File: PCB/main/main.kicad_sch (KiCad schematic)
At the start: 4 parts, among them J1 Conn_01x33_Female, J2 Conn_01x33_Female, J3 Conn_01x33_Female, J4 Conn_01x33_Female

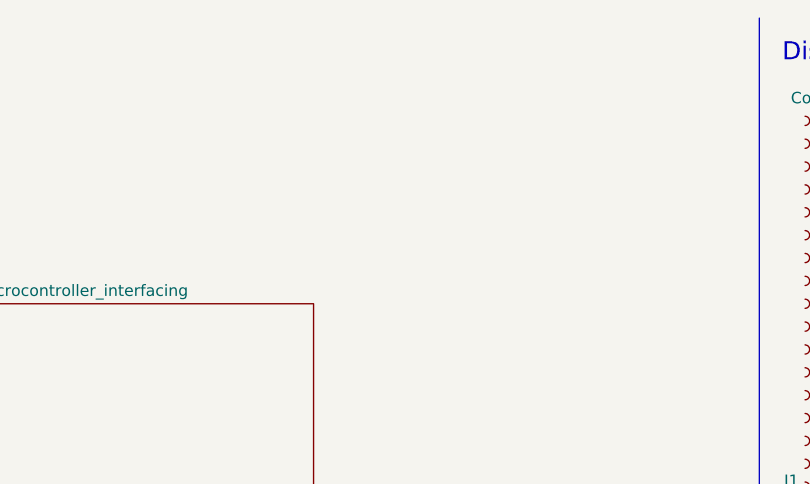
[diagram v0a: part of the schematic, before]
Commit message: Updated interfacing schem
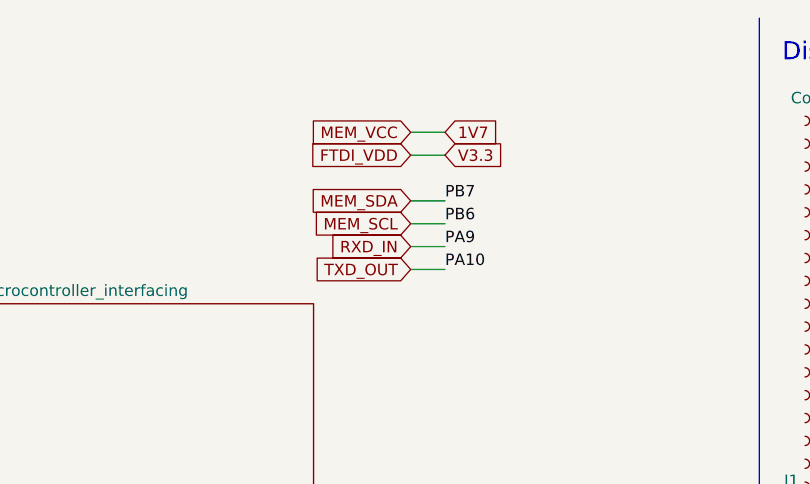
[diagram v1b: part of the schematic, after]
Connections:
- net PA10 renamed TXD_OUT
- net PA9 renamed RXD_IN
- net PB6 renamed MEM_SCL
- net PB7 renamed MEM_SDA
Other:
- title: EEE3088F Template -> EEE3088F Group 9
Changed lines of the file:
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@@
   (paper "A4")
   (title_block
-    (title "EEE3088F Template")
-    (date "2022-02-21")
-    (rev "V0.0")
+    (title "EEE3088F Group 9")
+    (date "2022-03-11")
+    (rev "V0.2")
     (company "University of Cape Town")
     (comment 3 "@Checked By: ")
-    (comment 4 "@Authors: Justin Pead")
+    (comment 4 "@Authors: David Young, Cameron Wilson, Caide Spriestersbach")
+  )
+  (wire (pts (xy 162.56 40.64) (xy 166.37 40.64))
+    (stroke (width 0) (type default) (color 0 0 0 0))
   )
   (wire (pts (xy 211.455 44.45) (xy 215.265 44.45))
     (stroke (width 0) (type default) (color 0 0 0 0))
   )
+  (wire (pts (xy 162.56 35.56) (xy 166.37 35.56))
+    (stroke (width 0) (type default) (color 0 0 0 0))
+  )
   (polyline (pts (xy 201.295 12.7) (xy 201.295 109.855))
     (stroke (width 0) (type default) (color 0 0 0 0))
@@
     (stroke (width 0) (type default) (color 0 0 0 0))
   )
+  (wire (pts (xy 162.56 38.1) (xy 166.37 38.1))
+    (stroke (width 0) (type default) (color 0 0 0 0))
+  )
   (wire (pts (xy 229.235 24.13) (xy 231.775 24.13))
     (stroke (width 0) (type default) (color 0 0 0 0))
@@
     (stroke (width 0) (type default) (color 0 0 0 0))
   )
+  (wire (pts (xy 162.56 27.94) (xy 166.37 27.94))
+    (stroke (width 0) (type default) (color 0 0 0 0))
+  )
+  (wire (pts (xy 162.56 33.02) (xy 166.37 33.02))
+    (stroke (width 0) (type default) (color 0 0 0 0))
+  )
   (wire (pts (xy 248.285 34.29) (xy 253.365 34.29))
+    (stroke (width 0) (type default) (color 0 0 0 0))
+  )
+  (wire (pts (xy 162.56 25.4) (xy 166.37 25.4))
     (stroke (width 0) (type default) (color 0 0 0 0))
   )
@@
     (effects (font (size 1.27 1.27)) (justify left bottom))
   )
+  (label "PA10" (at 166.37 40.64 0)
+    (effects (font (size 1.27 1.27)) (justify left bottom))
+  )
   (label "PC15" (at 211.455 36.83 0)
     (effects (font (size 1.27 1.27)) (justify left bottom))
@@
     (effects (font (size 1.27 1.27)) (justify left bottom))
   )
+  (label "PB6" (at 166.37 35.56 0)
+    (effects (font (size 1.27 1.27)) (justify left bottom))
+  )
   (label "PC0" (at 211.455 49.53 0)
     (effects (font (size 1.27 1.27)) (justify left bottom))
@@
     (effects (font (size 1.27 1.27)) (justify left bottom))
   )
+  (label "PB7" (at 166.37 33.02 0)
+    (effects (font (size 1.27 1.27)) (justify left bottom))
+  )
   (label "PA0" (at 229.235 59.69 0)
     (effects (font (size 1.27 1.27)) (justify left bottom))
@@
     (effects (font (size 1.27 1.27)) (justify left bottom))
   )
+  (label "PA9" (at 166.37 38.1 0)
+    (effects (font (size 1.27 1.27)) (justify left bottom))
+  )
   (label "PC9" (at 267.335 87.63 0)
     (effects (font (size 1.27 1.27)) (justify left bottom))
+  )
+  (global_label "FTDI_VDD" (shape input) (at 162.56 27.94 180) (fields_autoplaced)
+    (effects (font (size 1.27 1.27)) (justify right))
+    (property "Intersheet References" "${INTERSHEET_REFS}" (id 0) (at 151.6198 28.0194 0)
+      (effects (font (size 1.27 1.27)) (justify right) hide)
+    )
+  )
+  (global_label "1V7" (shape input) (at 166.37 25.4 0) (fields_autoplaced)
+    (effects (font (size 1.27 1.27)) (justify left))
+    (property "Intersheet References" "${INTERSHEET_REFS}" (id 0) (at 172.2907 25.3206 0)
+      (effects (font (size 1.27 1.27)) (justify left) hide)
+    )
+  )
+  (global_label "V3.3" (shape input) (at 166.37 27.94 0) (fields_autoplaced)
+    (effects (font (size 1.27 1.27)) (justify left))
+    (property "Intersheet References" "${INTERSHEET_REFS}" (id 0) (at 172.8955 27.8606 0)
+      (effects (font (size 1.27 1.27)) (justify left) hide)
+    )
+  )
+  (global_label "TXD_OUT" (shape input) (at 162.56 40.64 180) (fields_autoplaced)
+    (effects (font (size 1.27 1.27)) (justify right))
+    (property "Intersheet References" "${INTERSHEET_REFS}" (id 0) (at 152.1036 40.7194 0)
+      (effects (font (size 1.27 1.27)) (justify right) hide)
+    )
+  )
+  (global_label "RXD_IN" (shape input) (at 162.56 38.1 180) (fields_autoplaced)
+    (effects (font (size 1.27 1.27)) (justify right))
+    (property "Intersheet References" "${INTERSHEET_REFS}" (id 0) (at 153.4945 38.1794 0)
+      (effects (font (size 1.27 1.27)) (justify right) hide)
+    )
+  )
+  (global_label "MEM_VCC" (shape input) (at 162.56 25.4 180) (fields_autoplaced)
+    (effects (font (size 1.27 1.27)) (justify right))
+    (property "Intersheet References" "${INTERSHEET_REFS}" (id 0) (at 151.4988 25.3206 0)
+      (effects (font (size 1.27 1.27)) (justify right) hide)
+    )
+  )
+  (global_label "MEM_SCL" (shape input) (at 162.56 35.56 180) (fields_autoplaced)
+    (effects (font (size 1.27 1.27)) (justify right))
+    (property "Intersheet References" "${INTERSHEET_REFS}" (id 0) (at 151.6198 35.4806 0)
+      (effects (font (size 1.27 1.27)) (justify right) hide)
+    )
+  )
+  (global_label "MEM_SDA" (shape input) (at 162.56 33.02 180) (fields_autoplaced)
+    (effects (font (size 1.27 1.27)) (justify right))
+    (property "Intersheet References" "${INTERSHEET_REFS}" (id 0) (at 151.5593 32.9406 0)
+      (effects (font (size 1.27 1.27)) (justify right) hide)
+    )
   )
   (symbol (lib_id "power:GND") (at 233.045 105.41 90) (unit 1)
@@
       (reference "#PWR018") (unit 1) (value "GND") (footprint "")
     )
-    (path "/59b42903-2dc7-4011-ab5b-d7b81bd233c3/accade58-c1d2-4f6f-9fed-63e39d1d9928"
-      (reference "#PWR019") (unit 1) (value "GND") (footprint "")
-    )
     (path "/d15c8919-7ccc-44b2-8fc4-b04c1b47b6fa/dd448a84-e210-4674-86a8-ae65df0106f1"
       (reference "#PWR020") (unit 1) (value "GND") (footprint "")
@@
       (reference "R13") (unit 1) (value "4.7k") (footprint "")
     )
-    (path "/59b42903-2dc7-4011-ab5b-d7b81bd233c3/97b86286-2603-4849-bdd6-1cfc0a30163c"
-      (reference "R14") (unit 1) (value "10k") (footprint "")
-    )
     (path "/d15c8919-7ccc-44b2-8fc4-b04c1b47b6fa/0e943f16-1e71-4694-b072-e169f2da7d03"

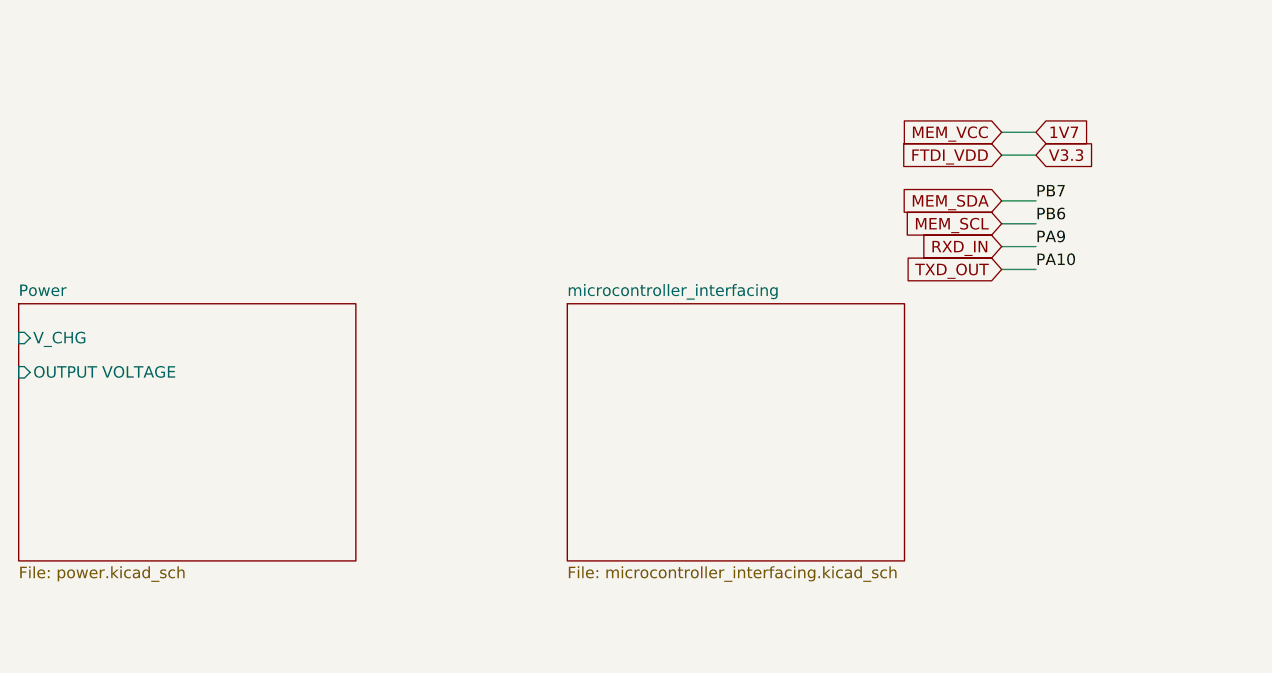
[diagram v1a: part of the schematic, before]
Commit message: Finished initial interfacing schem
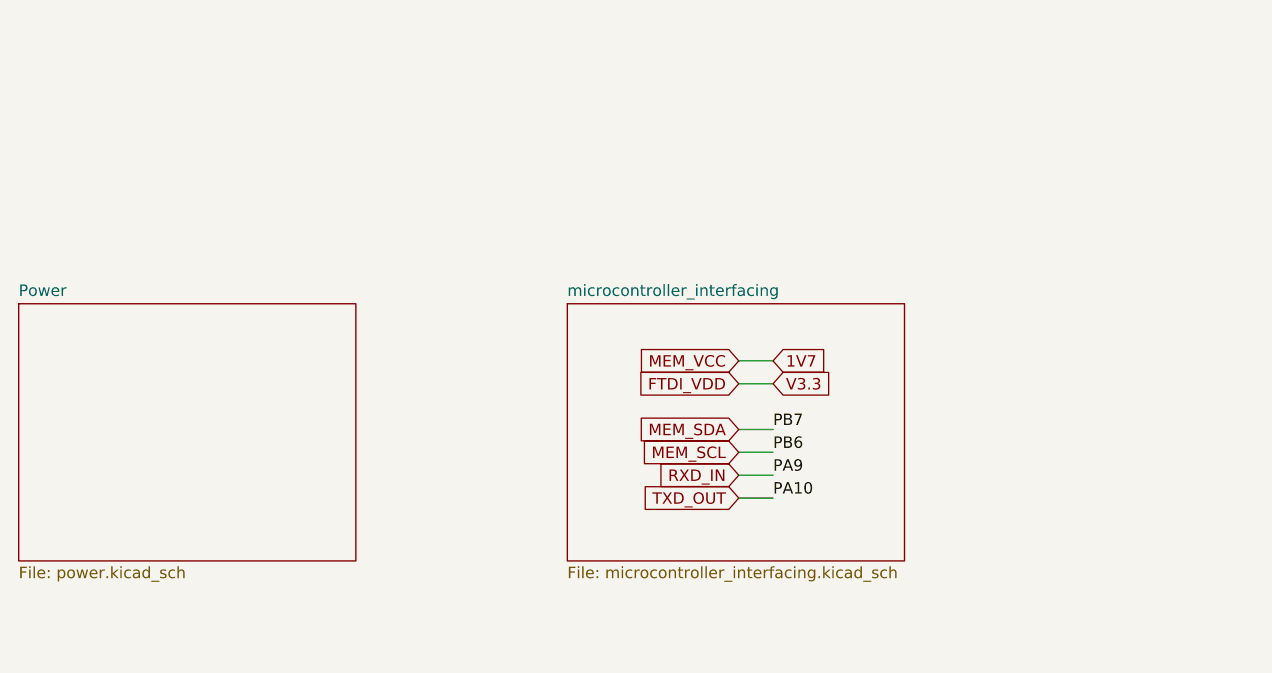
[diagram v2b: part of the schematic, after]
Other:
- sheet Power ports: added none; removed OUTPUT VOLTAGE, V_CHG
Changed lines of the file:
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@@
     (comment 4 "@Authors: David Young, Cameron Wilson, Caide Spriestersbach")
   )
-  (wire (pts (xy 162.56 40.64) (xy 166.37 40.64))
+  (wire (pts (xy 133.35 66.04) (xy 137.16 66.04))
     (stroke (width 0) (type default) (color 0 0 0 0))
   )
@@
     (stroke (width 0) (type default) (color 0 0 0 0))
   )
-  (wire (pts (xy 162.56 35.56) (xy 166.37 35.56))
+  (wire (pts (xy 133.35 60.96) (xy 137.16 60.96))
     (stroke (width 0) (type default) (color 0 0 0 0))
   )
@@
     (stroke (width 0) (type default) (color 0 0 0 0))
   )
-  (wire (pts (xy 162.56 38.1) (xy 166.37 38.1))
+  (wire (pts (xy 133.35 63.5) (xy 137.16 63.5))
     (stroke (width 0) (type default) (color 0 0 0 0))
   )
@@
     (stroke (width 0) (type default) (color 0 0 0 0))
   )
-  (wire (pts (xy 162.56 27.94) (xy 166.37 27.94))
-    (stroke (width 0) (type default) (color 0 0 0 0))
-  )
-  (wire (pts (xy 162.56 33.02) (xy 166.37 33.02))
+  (wire (pts (xy 133.35 53.34) (xy 137.16 53.34))
+    (stroke (width 0) (type default) (color 0 0 0 0))
+  )
+  (wire (pts (xy 133.35 58.42) (xy 137.16 58.42))
     (stroke (width 0) (type default) (color 0 0 0 0))
   )
@@
     (stroke (width 0) (type default) (color 0 0 0 0))
   )
-  (wire (pts (xy 162.56 25.4) (xy 166.37 25.4))
+  (wire (pts (xy 133.35 50.8) (xy 137.16 50.8))
     (stroke (width 0) (type default) (color 0 0 0 0))
   )
@@
     (effects (font (size 1.27 1.27)) (justify left bottom))
   )
-  (label "PA10" (at 166.37 40.64 0)
+  (label "PA10" (at 137.16 66.04 0)
     (effects (font (size 1.27 1.27)) (justify left bottom))
   )
@@
     (effects (font (size 1.27 1.27)) (justify left bottom))
   )
-  (label "PB6" (at 166.37 35.56 0)
+  (label "PB6" (at 137.16 60.96 0)
     (effects (font (size 1.27 1.27)) (justify left bottom))
   )
@@
     (effects (font (size 1.27 1.27)) (justify left bottom))
   )
-  (label "PB7" (at 166.37 33.02 0)
+  (label "PB7" (at 137.16 58.42 0)
     (effects (font (size 1.27 1.27)) (justify left bottom))
   )
@@
     (effects (font (size 1.27 1.27)) (justify left bottom))
   )
-  (label "PA9" (at 166.37 38.1 0)
+  (label "PA9" (at 137.16 63.5 0)
     (effects (font (size 1.27 1.27)) (justify left bottom))
   )
@@
     (effects (font (size 1.27 1.27)) (justify left bottom))
   )
-  (global_label "FTDI_VDD" (shape input) (at 162.56 27.94 180) (fields_autoplaced)
+  (global_label "FTDI_VDD" (shape input) (at 133.35 53.34 180) (fields_autoplaced)
     (effects (font (size 1.27 1.27)) (justify right))
-    (property "Intersheet References" "${INTERSHEET_REFS}" (id 0) (at 151.6198 28.0194 0)
+    (property "Intersheet References" "${INTERSHEET_REFS}" (id 0) (at 122.4098 53.4194 0)
       (effects (font (size 1.27 1.27)) (justify right) hide)
     )
   )
-  (global_label "1V7" (shape input) (at 166.37 25.4 0) (fields_autoplaced)
+  (global_label "1V7" (shape input) (at 137.16 50.8 0) (fields_autoplaced)
     (effects (font (size 1.27 1.27)) (justify left))
-    (property "Intersheet References" "${INTERSHEET_REFS}" (id 0) (at 172.2907 25.3206 0)
+    (property "Intersheet References" "${INTERSHEET_REFS}" (id 0) (at 143.0807 50.7206 0)
       (effects (font (size 1.27 1.27)) (justify left) hide)
     )
   )
-  (global_label "V3.3" (shape input) (at 166.37 27.94 0) (fields_autoplaced)
+  (global_label "V3.3" (shape input) (at 137.16 53.34 0) (fields_autoplaced)
     (effects (font (size 1.27 1.27)) (justify left))
-    (property "Intersheet References" "${INTERSHEET_REFS}" (id 0) (at 172.8955 27.8606 0)
+    (property "Intersheet References" "${INTERSHEET_REFS}" (id 0) (at 143.6855 53.2606 0)
       (effects (font (size 1.27 1.27)) (justify left) hide)
     )
   )
-  (global_label "TXD_OUT" (shape input) (at 162.56 40.64 180) (fields_autoplaced)
+  (global_label "TXD_OUT" (shape input) (at 133.35 66.04 180) (fields_autoplaced)
     (effects (font (size 1.27 1.27)) (justify right))
-    (property "Intersheet References" "${INTERSHEET_REFS}" (id 0) (at 152.1036 40.7194 0)
+    (property "Intersheet References" "${INTERSHEET_REFS}" (id 0) (at 122.8936 66.1194 0)
       (effects (font (size 1.27 1.27)) (justify right) hide)
     )
   )
-  (global_label "RXD_IN" (shape input) (at 162.56 38.1 180) (fields_autoplaced)
+  (global_label "RXD_IN" (shape input) (at 133.35 63.5 180) (fields_autoplaced)
     (effects (font (size 1.27 1.27)) (justify right))
-    (property "Intersheet References" "${INTERSHEET_REFS}" (id 0) (at 153.4945 38.1794 0)
+    (property "Intersheet References" "${INTERSHEET_REFS}" (id 0) (at 124.2845 63.5794 0)
       (effects (font (size 1.27 1.27)) (justify right) hide)
     )
   )
-  (global_label "MEM_VCC" (shape input) (at 162.56 25.4 180) (fields_autoplaced)
+  (global_label "MEM_VCC" (shape input) (at 133.35 50.8 180) (fields_autoplaced)
     (effects (font (size 1.27 1.27)) (justify right))
-    (property "Intersheet References" "${INTERSHEET_REFS}" (id 0) (at 151.4988 25.3206 0)
+    (property "Intersheet References" "${INTERSHEET_REFS}" (id 0) (at 122.2888 50.7206 0)
       (effects (font (size 1.27 1.27)) (justify right) hide)
     )
   )
-  (global_label "MEM_SCL" (shape input) (at 162.56 35.56 180) (fields_autoplaced)
+  (global_label "MEM_SCL" (shape input) (at 133.35 60.96 180) (fields_autoplaced)
     (effects (font (size 1.27 1.27)) (justify right))
-    (property "Intersheet References" "${INTERSHEET_REFS}" (id 0) (at 151.6198 35.4806 0)
+    (property "Intersheet References" "${INTERSHEET_REFS}" (id 0) (at 122.4098 60.8806 0)
       (effects (font (size 1.27 1.27)) (justify right) hide)
     )
   )
-  (global_label "MEM_SDA" (shape input) (at 162.56 33.02 180) (fields_autoplaced)
+  (global_label "MEM_SDA" (shape input) (at 133.35 58.42 180) (fields_autoplaced)
     (effects (font (size 1.27 1.27)) (justify right))
-    (property "Intersheet References" "${INTERSHEET_REFS}" (id 0) (at 151.5593 32.9406 0)
+    (property "Intersheet References" "${INTERSHEET_REFS}" (id 0) (at 122.3493 58.3406 0)
       (effects (font (size 1.27 1.27)) (justify right) hide)
     )
@@
       (effects (font (size 1.27 1.27)) (justify left top))
     )
-    (pin "V_CHG" input (at 53.34 48.26 180)
-      (effects (font (size 1.27 1.27)) (justify left))
-    )
-    (pin "OUTPUT VOLTAGE" input (at 53.34 52.07 180)
-      (effects (font (size 1.27 1.27)) (justify left))
-    )
-  )
+  )
